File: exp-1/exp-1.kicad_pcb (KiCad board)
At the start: 4 copper layers, 50.8 x 50.8 mm, 126 parts, among them Q1 2n5109, Q2 MMBT3904T, Q3 MMBT3904T, Q4 DMP3099L, Q5 MMBT3904T, Q6 DMP3099L, U1 ABA-52563, U2 AVT-50663, U3 ABA-52563, U4 AVT-50663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

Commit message: Continued work on that one thing
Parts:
- added P1: CONN_8, exp-1:2x4_EDGE_.1, F.Cu at (47.2, 116.8)
- added U9: MCP1703T, Housings_SOT-23_SOT-143_TSOT-6:SOT-23, B.Cu at (91.9, 115.3)
- moved C49 75.5 mm to (91.9, 111.8), turned to 180 degrees
- moved R21 71.8 mm to (93.0, 121.3), turned to 270 degrees
- moved R24 67.7 mm to (106.7, 121.9), turned to 270 degrees
- moved R19 66.2 mm to (97.0, 128.0), turned to 270 degrees
- moved R20 65.3 mm to (100.1, 121.9), turned to 270 degrees
- moved R17 62.2 mm to (94.5, 128.0), turned to 90 degrees
- moved R18 61.2 mm to (103.6, 128.0), turned to 270 degrees
- moved Q6 60.0 mm to (109.7, 119.4), turned to 180 degrees
- moved R22 59.9 mm to (107.7, 128.0), turned to 90 degrees
- moved Q4 59.3 mm to (103.1, 119.4), turned to 180 degrees
- moved R16 59.1 mm to (101.1, 128.0), turned to 90 degrees
- moved R23 58.4 mm to (110.2, 128.0), turned to 270 degrees
- moved Q3 54.9 mm to (96.0, 123.4), turned to 180 degrees
- moved Q5 42.2 mm to (110.8, 123.0), turned to 180 degrees
- moved Q2 41.4 mm to (103.1, 123.4), turned to 180 degrees
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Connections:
- C49 pad 1: Net-(C49-Pad1) -> +3.3V
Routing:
- net /10V: track 3.91 -> 33.1 mm, vias 0 -> 2
- net /VATEN: track 0.00 -> 21.5 mm
- net GND: track 297.8 -> 318.7 mm, vias 52 -> 55
- net Net-(D3-Pad2): track 0.00 -> 16.0 mm
- net Net-(C36-Pad1): track 7.50 -> 20.4 mm
- net +3.3V: track 32.3 -> 44.6 mm
- net /VTX: track 7.65 -> 16.4 mm, vias 0 -> 1
- net Net-(Q2-Pad1): track 0.00 -> 7.63 mm
- net /EN_RX: track 0.00 -> 7.62 mm
- net Net-(Q3-Pad1): track 0.00 -> 7.39 mm
- net Net-(Q5-Pad3): track 0.00 -> 6.29 mm
- net Net-(Q2-Pad3): track 0.00 -> 5.74 mm
- net Net-(C38-Pad2): track 6.40 -> 9.24 mm

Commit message: more routing
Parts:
- moved P1 30.7 mm to (75.7, 105.4), turned to 0 degrees
- moved U8 3.78 mm to (79.5, 114.8)
- moved C47 2.27 mm to (87.4, 106.7), turned to 90 degrees
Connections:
- FILT3 pad 3: /RATT2 -> /RATT_2
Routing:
- net /EN_TX: track 0.00 -> 59.6 mm, vias 0 -> 2
- net /RATT_2: track 4.70 -> 53.6 mm, vias 0 -> 3
- net /ATSC: track 0.00 -> 41.3 mm
- net /ATRC: track 0.00 -> 39.7 mm, vias 0 -> 1
- net /ATD: track 0.00 -> 37.4 mm, vias 0 -> 1
- net /EN_RX: track 7.62 -> 44.0 mm, vias 0 -> 3
- net /RATT_1: track 4.80 -> 36.9 mm, vias 0 -> 1
- net /SDA: track 3.78 -> 33.3 mm, vias 0 -> 2
- net +3.3V: track 44.6 -> 67.6 mm
- net /SCL: track 4.03 -> 25.8 mm, vias 0 -> 1
- net /VATEN: track 21.5 -> 41.3 mm
- net /VRX: track 0.00 -> 12.3 mm
- net GND: track 318.7 -> 327.4 mm, vias 55 -> 58
- net /VIN: track 3.40 -> 7.04 mm
- net /10V: track 33.1 -> 36.5 mm
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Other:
- net class DSig added: clearance 0.1524, trace_width 0.1778, via_dia 0.635, via_drill 0.4064
- net class Default: clearance 0.2032 -> 0.1524
- rule trace_clearance: 0.2032 -> 0.1524

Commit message: Schematic probably done. Layout still needs work
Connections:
- FILT3 pad 3: /RATT_2 -> /RATT2
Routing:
- net /RATT_2: track 53.6 -> 45.6 mm
- net /RATT2: track 0.00 -> 7.98 mm

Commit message: Further work on that one thing
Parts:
- added P2: BNC, exp-1:SMA_EMNT, F.Cu at (122.4, 121.4)
- added P4: BNC, exp-1:SMA_EMNT, F.Cu at (122.4, 134.9)
- moved C30 3.10 mm to (118.4, 142.3)
- moved C28 2.09 mm to (115.8, 143.3)
- moved C29 2.09 mm to (115.8, 141.2)
- moved C46 1.20 mm to (122.7, 111.3)
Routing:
- net Net-(C10-Pad1): track 45.7 -> 8.70 mm, vias 1 -> 0
- net GND: track 327.4 -> 359.7 mm, vias 58 -> 57
- net /RATT_2: track 45.6 -> 50.9 mm
- net /RATT2: track 7.98 -> 2.61 mm
- net Net-(C26-Pad1): track 10.7 -> 9.38 mm
- net /TX_P: track 12.8 -> 12.1 mm

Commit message: More of the same
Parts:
- moved SL1 2.50 mm to (116.8, 131.4)
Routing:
- net /RATT_2: track 50.9 -> 7.96 mm, vias 3 -> 2
- net /RATT2: track 2.61 -> 45.6 mm, vias 0 -> 1
- net /VTX: track 19.8 -> 62.5 mm, vias 1 -> 3
- net Net-(C10-Pad1): track 8.70 -> 43.3 mm, vias 0 -> 1
- net GND: track 359.7 -> 329.8 mm, vias 57 -> 76
- net /VRX: track 12.3 -> 30.7 mm, vias 0 -> 1
- net Net-(C38-Pad1): track 0.00 -> 12.4 mm
- net Net-(P4-Pad1): track 0.00 -> 6.56 mm
- net Net-(C46-Pad2): track 0.00 -> 3.73 mm
- net /SDA: track 33.3 -> 36.0 mm
- net /TX_SL: track 14.8 -> 12.6 mm
- net /EN_RX: track 44.0 -> 45.6 mm
- net /TX_P: track 12.1 -> 13.5 mm
- net (no net): track 0.00 -> 1.08 mm
- added copper zone on F.Cu, net GND

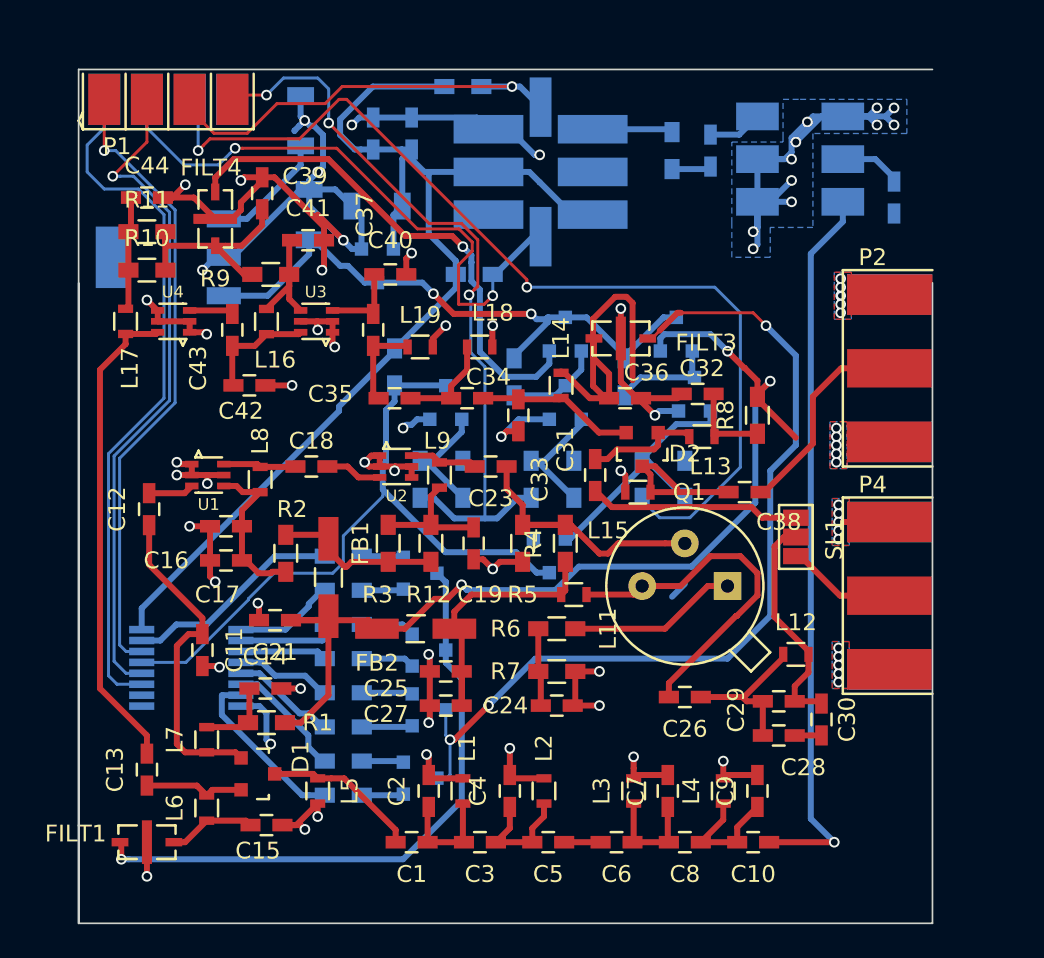
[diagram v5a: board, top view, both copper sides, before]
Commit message: Added the rest of the connectors
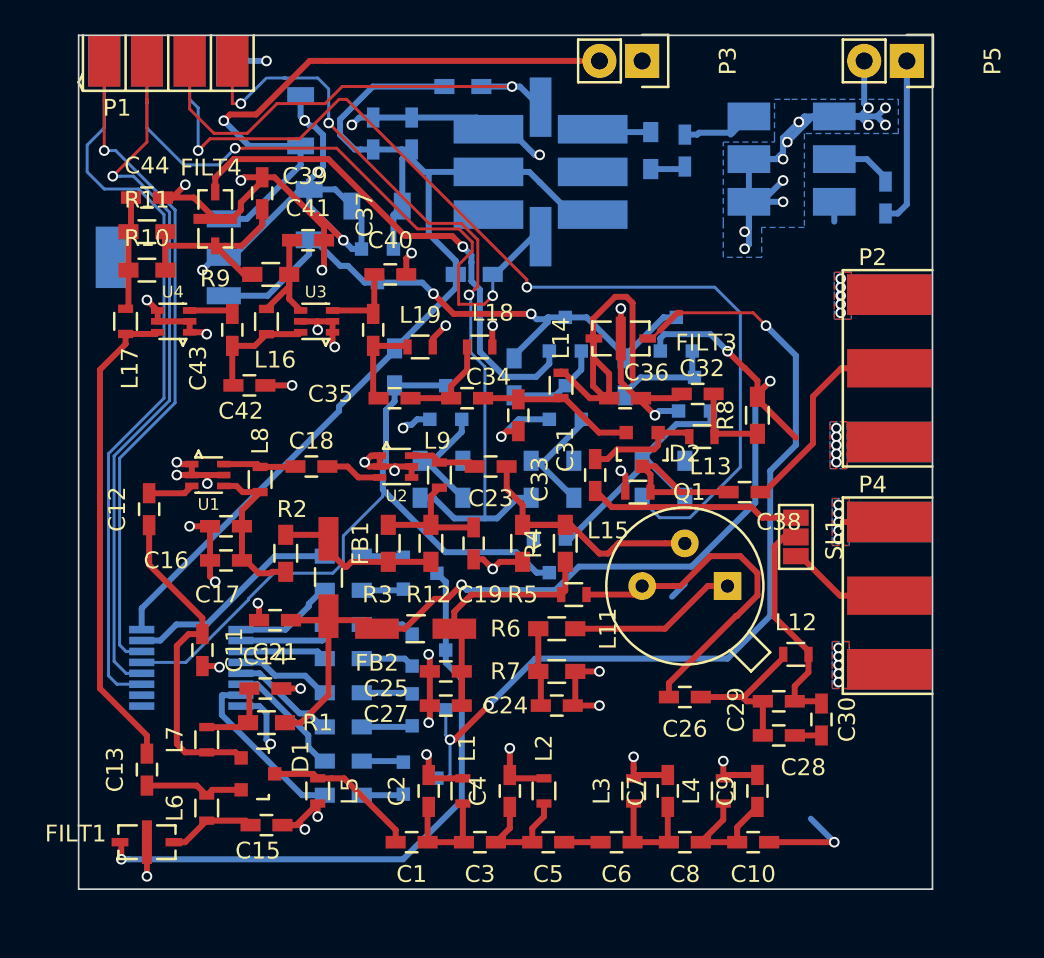
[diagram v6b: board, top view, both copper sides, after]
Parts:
- added P3: CONN_2, Pin_Headers:Pin_Header_Straight_1x02, F.Cu at (107.7, 103.1)
- added P5: CONN_2, Pin_Headers:Pin_Header_Straight_1x02, F.Cu at (123.4, 103.1)
- P2, P4: value BNC -> SMA
- moved P1 2.29 mm to (75.7, 103.1)
- moved C45 1.52 mm to (110.2, 108.5)
- moved R15 1.27 mm to (108.2, 108.5)
- moved C46 0.51 mm to (122.2, 111.3)
- moved U5 0.51 mm to (119.1, 106.4)
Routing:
- net /RATT_2: track 7.96 -> 52.7 mm, vias 2 -> 3
- net /RATT2: track 45.6 -> 0.86 mm, vias 1 -> 0
- net Net-(C10-Pad1): track 43.3 -> 7.03 mm
- net /VIN: track 7.04 -> 36.1 mm, vias 0 -> 1
- net GND: track 329.8 -> 347.6 mm, vias 76 -> 62
- net /IF: track 0.00 -> 10.0 mm
- net /EN_RX: track 45.6 -> 48.2 mm
- net /SDA: track 36.0 -> 38.5 mm
- net /ATD: track 37.4 -> 39.9 mm
- net /ATRC: track 39.7 -> 42.1 mm
- net /SCL: track 25.5 -> 27.8 mm
- net /EN_TX: track 59.2 -> 61.4 mm
- net /ATSC: track 41.3 -> 43.6 mm
- net Net-(R15-Pad2): track 4.79 -> 3.52 mm
- net /LO: track 3.24 -> 4.42 mm
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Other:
- outline, holes or cut-outs redrawn

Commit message: Further layout work
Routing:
- net /RATT_2: track 52.7 -> 7.96 mm, vias 3 -> 1
- net /RATT2: track 0.86 -> 45.6 mm, vias 0 -> 2
- net Net-(C10-Pad1): track 7.03 -> 40.0 mm
- net GND: track 347.6 -> 348.9 mm, vias 62 -> 63

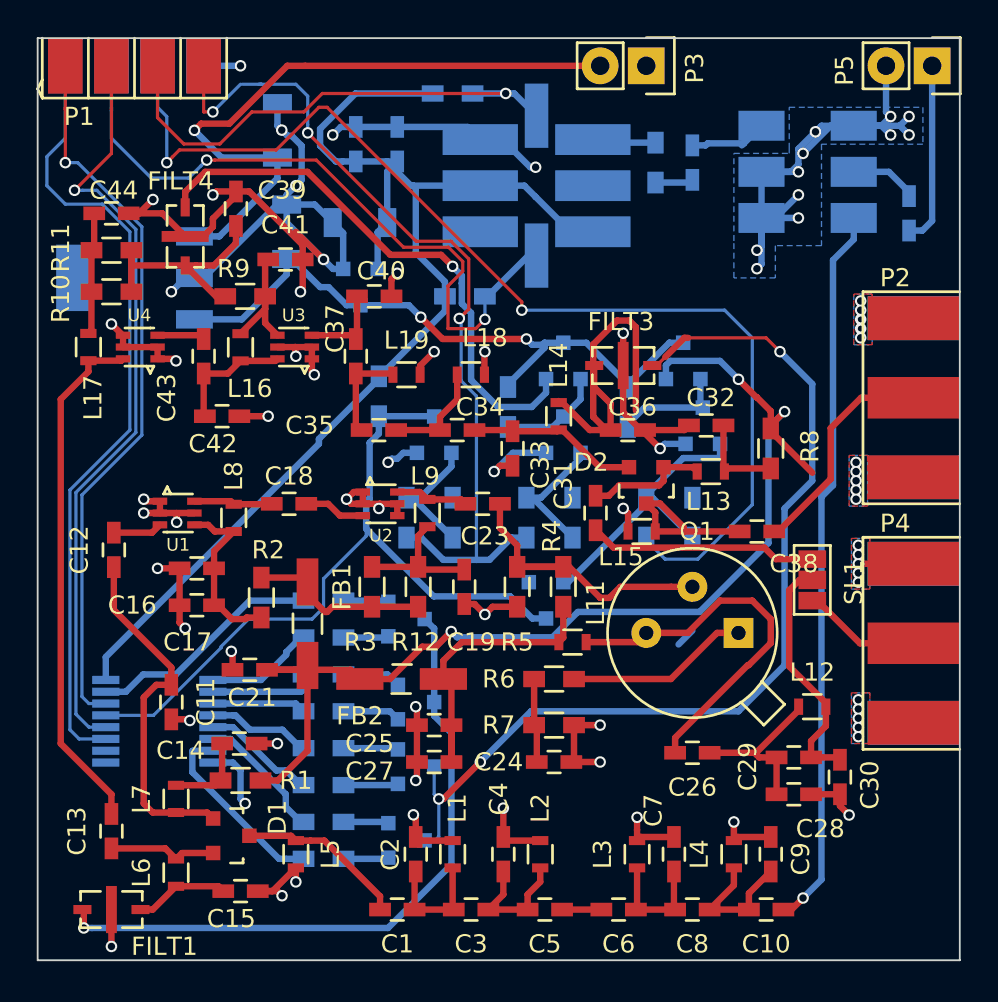
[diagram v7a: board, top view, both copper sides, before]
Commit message: Replaced power switching with canned switch. Changed 10v regulator to 5v.
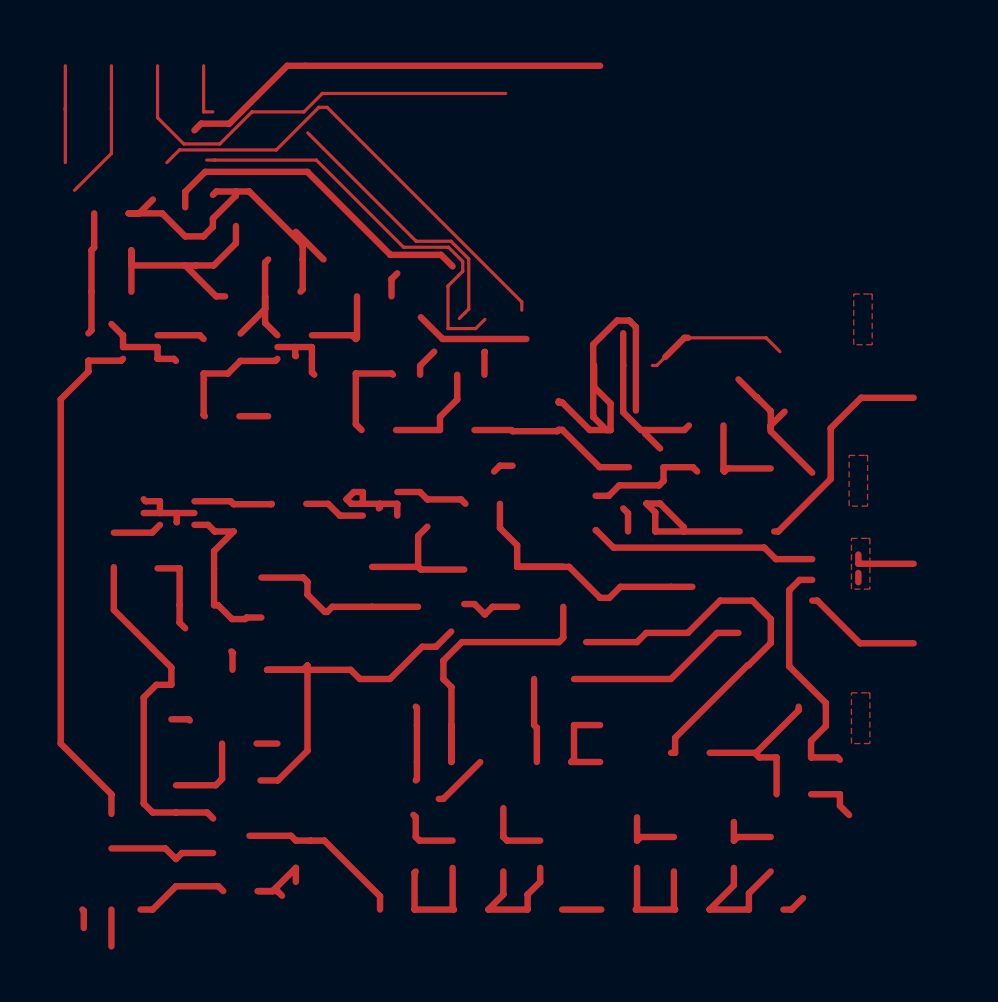
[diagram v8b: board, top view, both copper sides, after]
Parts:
- removed C1, C10: 2.7p, Capacitors_SMD:C_0603_HandSoldering
- removed C11, C26, C28, C30: 15p, Capacitors_SMD:C_0603_HandSoldering
- removed C12, C13, C18, C23, C31, C38, C43, C45, C46: 470p, Capacitors_SMD:C_0603_HandSoldering
- removed C14, C15, C16, C17, C19, C20, C21, C22, C24, C25, C27, C32, C36, C39, C41, C44: .01u, Capacitors_SMD:C_0603_HandSoldering
- removed C2, C29, C9: 8.2p, Capacitors_SMD:C_0603_HandSoldering
- removed C3, C5, C8: .5p, Capacitors_SMD:C_0603_HandSoldering
- removed C33, C40: 47p, Capacitors_SMD:C_0603_HandSoldering
- removed C34, C37, C4, C7: 12p, Capacitors_SMD:C_0603_HandSoldering
- removed C35, C6: 1p, Capacitors_SMD:C_0603_HandSoldering
- removed C42: 33p, Capacitors_SMD:C_0603_HandSoldering
- removed C47, C48, C49: 22u, Capacitors_SMD:C_1206
- removed D1, D2: BAR15-1, Housings_SOT-23_SOT-143_TSOT-6:SOT-23
- removed D3, D4, D5, D6, D7: BAT54C, Housings_SOT-23_SOT-143_TSOT-6:SOT-23
- removed FB1, FB2: FILTER, Choke_SMD:Choke_SMD_1206_Handsoldering
- removed FILT1, FILT3, FILT4: MTFILT, exp-1:FILTACH32T
- removed L1, L11, L18, L19, L4: 100n, Resistors_SMD:R_0603
- removed L12: 39n, Resistors_SMD:R_0603
- removed L13, L14, L15, L16, L17, L5, L6, L7, L8, L9: .33u, Resistors_SMD:R_0603
- removed L2, L3: 91n, Resistors_SMD:R_0603
- removed P1: CONN_8, exp-1:2x4_EDGE_.1
- removed P2, P4: SMA, exp-1:SMA_EMNT
- removed P3, P5: CONN_2, Pin_Headers:Pin_Header_Straight_1x02
- removed Q1: 2n5109, Discret:TO39EBC
- removed Q2, Q3, Q5: MMBT3904T, Housings_SOT-23_SOT-143_TSOT-6:SOT-23
- removed Q4, Q6: DMP3099L, Housings_SOT-23_SOT-143_TSOT-6:SOT-23
- removed R1, R8: 680R, Resistors_SMD:R_0603_HandSoldering
- removed R10, R11, R12, R3: 331R, Resistors_SMD:R_0603_HandSoldering
- removed R13, R14, R16, R17, R22, R5: 1K, Resistors_SMD:R_0603_HandSoldering
- removed R15: 38R, Resistors_SMD:R_0603_HandSoldering
- removed R18, R19, R20, R23, R24: 10K, Resistors_SMD:R_0603_HandSoldering
- removed R2, R9: 121R, Resistors_SMD:R_0603_HandSoldering
- removed R21: 1k, Resistors_SMD:R_0603_HandSoldering
- removed R25, R29: 300, Resistors_SMD:R_0603_HandSoldering
- removed R26, R30: 6.2k, Resistors_SMD:R_0603_HandSoldering
- removed R27, R31: 20k, Resistors_SMD:R_0603_HandSoldering
- removed R28, R32: 47k, Resistors_SMD:R_0603_HandSoldering
- removed R4: 3.3k, Resistors_SMD:R_0603_HandSoldering
- removed R6: 2.2R, Resistors_SMD:R_0603_HandSoldering
- removed R7: 22R, Resistors_SMD:R_0603_HandSoldering
- removed SL1: SDRSEL, exp-1:BSEL2
- removed U1, U3: ABA-52563, exp-1:SOT_363
- removed U2, U4: AVT-50663, exp-1:SOT_363
- removed U5: ADE-1, exp-1:PL-052
- removed U6: Si570, exp-1:SI570-HS
- removed U7: 74HC595_, Housings_SSOP:TSSOP-16_4.4x5mm_Pitch0.65mm
- removed U8: LM2937, SMD_Packages:SOT-223
- removed U9: MCP1703T, Housings_SOT-23_SOT-143_TSOT-6:SOT-23
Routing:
- net (no net): track 1.44 -> 675.0 mm, vias 15 -> 0
- net GND: track 348.9 -> 0.00 mm, vias 63 -> 0
- net +3.3V: track 67.6 -> 0.00 mm
- net /VTX: track 62.5 -> 0.00 mm, vias 3 -> 0
- net /EN_TX: track 61.4 -> 0.00 mm, vias 2 -> 0
- net /EN_RX: track 48.2 -> 0.00 mm, vias 3 -> 0
- net /RATT2: track 45.6 -> 0.00 mm, vias 2 -> 0
- net /ATSC: track 43.6 -> 0.00 mm
- net /ATRC: track 42.1 -> 0.00 mm, vias 1 -> 0
- net /VATEN: track 41.3 -> 0.00 mm
- net Net-(C10-Pad1): track 40.0 -> 0.00 mm, vias 1 -> 0
- net /ATD: track 39.9 -> 0.00 mm, vias 1 -> 0
- net /SDA: track 38.5 -> 0.00 mm, vias 2 -> 0
- net /RATT_1: track 36.9 -> 0.00 mm, vias 1 -> 0
- net /10V: track 36.5 -> 0.00 mm, vias 2 -> 0
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- removed copper zone on B.Cu, net GND
- removed copper zone on In1.Cu, net GND
- removed copper zone on In2.Cu, net GND
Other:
- board outline removed
